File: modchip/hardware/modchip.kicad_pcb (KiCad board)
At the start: 2 copper layers, 106.2 x 37.2 mm, 4 parts, among them J1 To switch T3 (I2C slave), J2 To switch T8 (GPIO46-49), J3 To switch T5 (UART0)

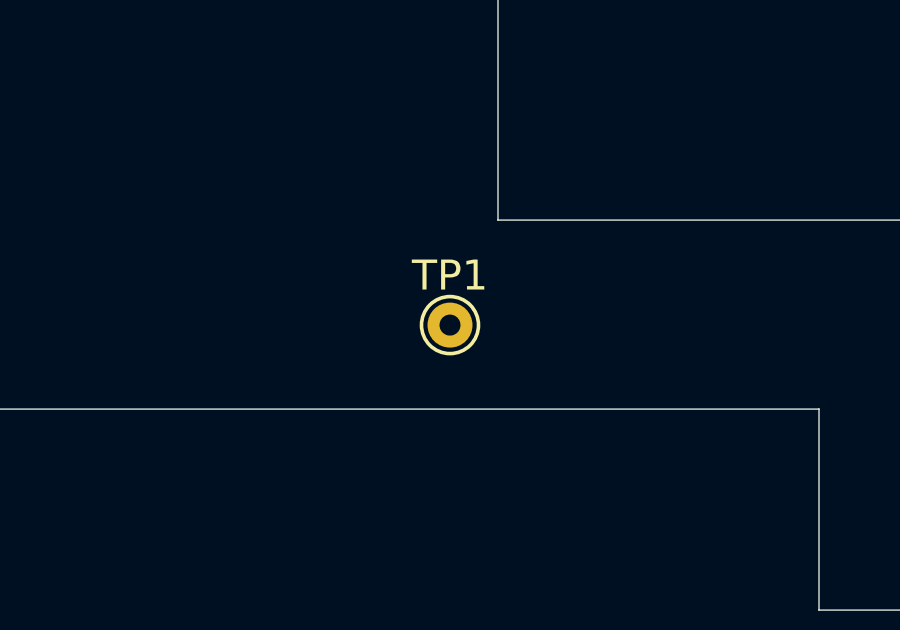
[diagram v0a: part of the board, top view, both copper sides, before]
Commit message: modchip: switch to the RP2350; wire the reset to D3's anode
The design moves from the RP2040 to the RP2350 (RP2354A, with 2 MiB of flash
in the package, or RP2350A with a W25Q16JV): a hardware RNG, SHA-256
acceleration, OTP for keys and 520 KB of SRAM make HTTPS practical. The
architecture doc covers the on-chip switching regulator's inductor, the
four-layer stack, erratum E9 and the UART divisors from a 150 MHz clk_peri.
Pin assignments are unchanged; the Pico scripts run on a Pico 2 as well.

The doc placed the reset line at D3's cathode. In this RC reset the
cathode (the banded rear end) sits on the 3.3 V rail, and pulling it low
would short the supply. The reset node is the anode, the front pad beside
the "+". The doc now says so, describes the meter check (0 ohm vs 33 kOhm
to 3.3 V), and adds 1 kOhm in series with the driver so a misplaced wire
can't short the rail. TP1 moves to 1 mm closer to the anode pad.

Co-Authored-By: Claude Opus 5.5 <noreply@anthropic.com>
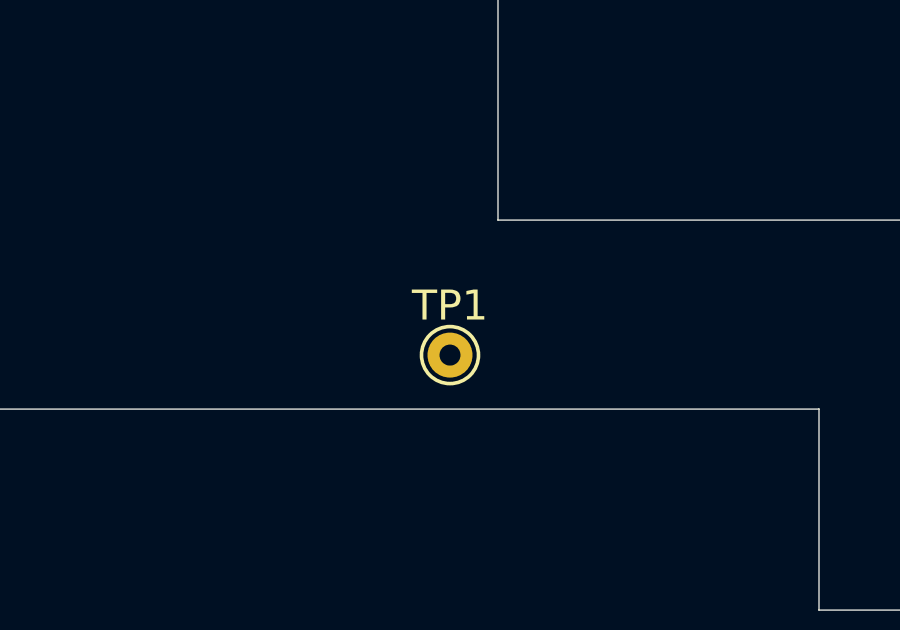
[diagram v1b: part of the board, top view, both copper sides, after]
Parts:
- TP1: value Reset wire to D3 -> Reset: wire to D3 anode (front pad, + end)
- moved TP1 1.00 mm to (120.2, 56.0)
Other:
- board text added: "TP1: wire to D3's ANODE (front pad, by the +), never the banded end (3.3 V rail). 1 k in series in the driver."

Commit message: modchip: KiCad 10 schematic of the RP2350 mod chip
make_sch.py generates modchip.kicad_sch from tables that give the net of
every pin of every part, with symbols from KiCad 10's standard library
(flattened as KiCad embeds them) and global labels named as on the board.
check_sch.py runs ERC and compares KiCad's netlist pin by pin with
expected-nets.json: all 240 pins match, and the only ERC error is the
intended one, the two LM66100 ideal diodes both driving +3V3.

The circuit: RP2354A with the core regulator from the datasheet's figure
22, a 12 MHz crystal, BOOTSEL/RUN, SWD and a status LED; USB-C with ESD
protection and an AP2112K-3.3, ORed with the switch's 3.3 V by two
LM66100; a sense divider on GP26; 100 R on every switch line, I2C
pull-ups to the switch's rail; the reset driver with 1 k to TP1.

U5 (W25Q16JVUXIQ) and C19 sit on the QSPI bus as DNP: fit them only with an
RP2350A. The RP2354A's internal flash is wired to the same QSPI pads
(RP2350 datasheet 14.3), so fitting both would put two chips on one chip
select.

make_pcb.py now links J1-J3 and TP1 to their symbols and copies their
fields, makes the board four layers and leaves J3 pin 4 open, so Update
PCB from Schematic adds the remaining parts without touching those four.

Co-Authored-By: Claude Opus 5.5 <noreply@anthropic.com>
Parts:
- J1, J2: footprint PinHeader_1x06_P2.00mm_Vertical -> Connector_PinHeader_2.00mm:PinHeader_1x06_P2.00mm_Vertical
- J3: footprint PinHeader_1x04_P2.54mm_Vertical -> Connector_PinHeader_2.54mm:PinHeader_1x04_P2.54mm_Vertical
- TP1: value Reset: wire to D3 anode (front pad, + end) -> Reset wire to D3 anode; footprint TestPoint_THTPad_D1.5mm_Drill0.7mm -> TestPoint:TestPoint_THTPad_D1.5mm_Drill0.7mm
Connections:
- J3 pad 4: +3V3_SW -> (no net)
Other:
- copper layers 2 -> 4

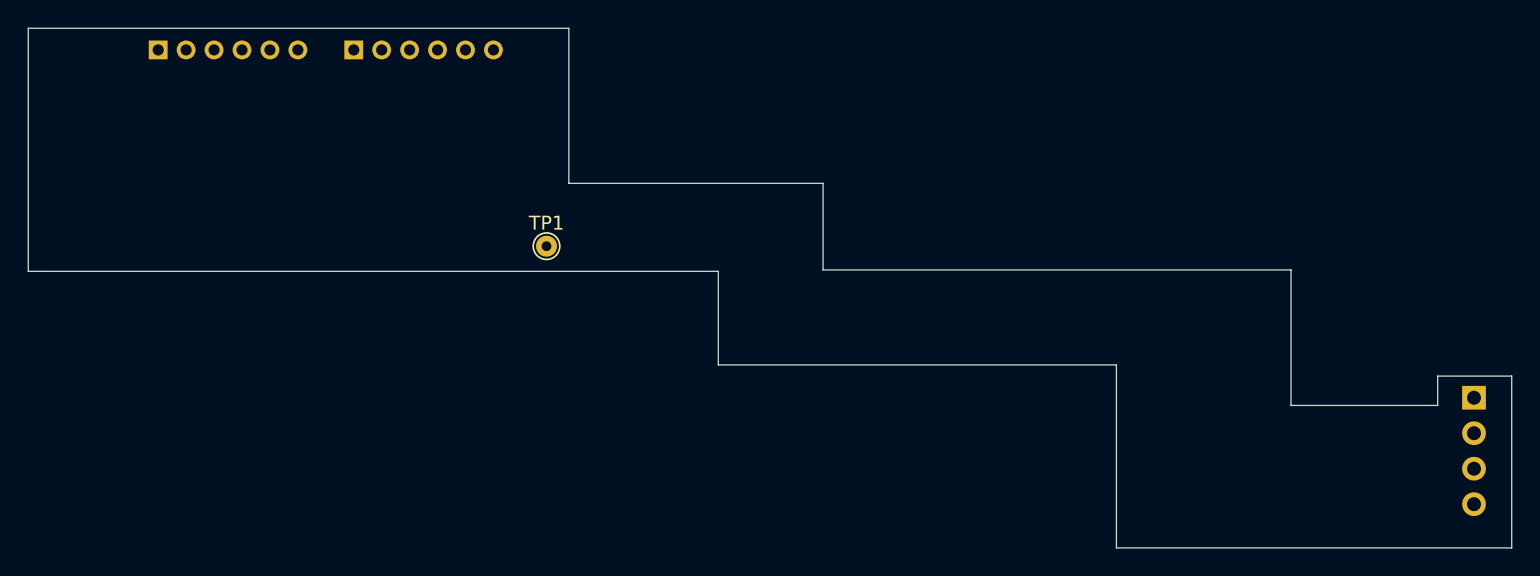
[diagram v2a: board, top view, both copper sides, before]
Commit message: modchip: route the RP2350 board and generate JLCPCB production files
Layout and routing, built by modchip/hardware/build.sh with kicad-agent-kit
(board from netlist, placement, plane fanout, Freerouting, A* finisher):

- 4 layers: F.Cu parts and signals, In1 GND, In2 +3V3, B.Cu signals; only
  the hand-soldered headers on the bottom.
- GPIOs follow the board: U1 rotated 270 puts GP11..GP0 under T3/T8 in
  header order (I2C on I2C1, GP11/GP10; T8 on GP7..GP4; UART GP0/GP1;
  reset GP27; LED GP22), so the fan-out doesn't cross.
- Hand routes laid before the router: VREG_LX and VREG_AVDD, the +3V3 trunk
  to CIN, the +1V1 DVDD pins on vias and B.Cu tracks round the exposed pad,
  the T8 fan and UART lanes, and a few boxed-in plane vias. Escape corridors
  round U1 stay clear of auto-placed parts.
- KiCad DRC: no errors, no warnings, schematic parity included.

Circuit changes on the way: no USB (SWD on J5 programs, debugs and can
power the board, the LM66100 keeping that supply out of the switch); the
RP2350A with a W25Q128JVSIQ is the default build, an RP2354A without U5/C19
the alternative; every part has an LCSC number, Basic wherever one exists,
with four in-stock Extended parts (RP2350A, LM66100, the datasheet's AOTA
inductor, the ABM8 crystal the RP2350 is tuned for); headers are not
assembled. Fixed on the way: L1's fields were passed as its DNP flag.

production/ holds the Gerber/drill zip, BOM (19 lines) and placement file
(48 parts, top side only) from the Fabrication Toolkit.

Co-Authored-By: Claude Opus 5.5 <noreply@anthropic.com>
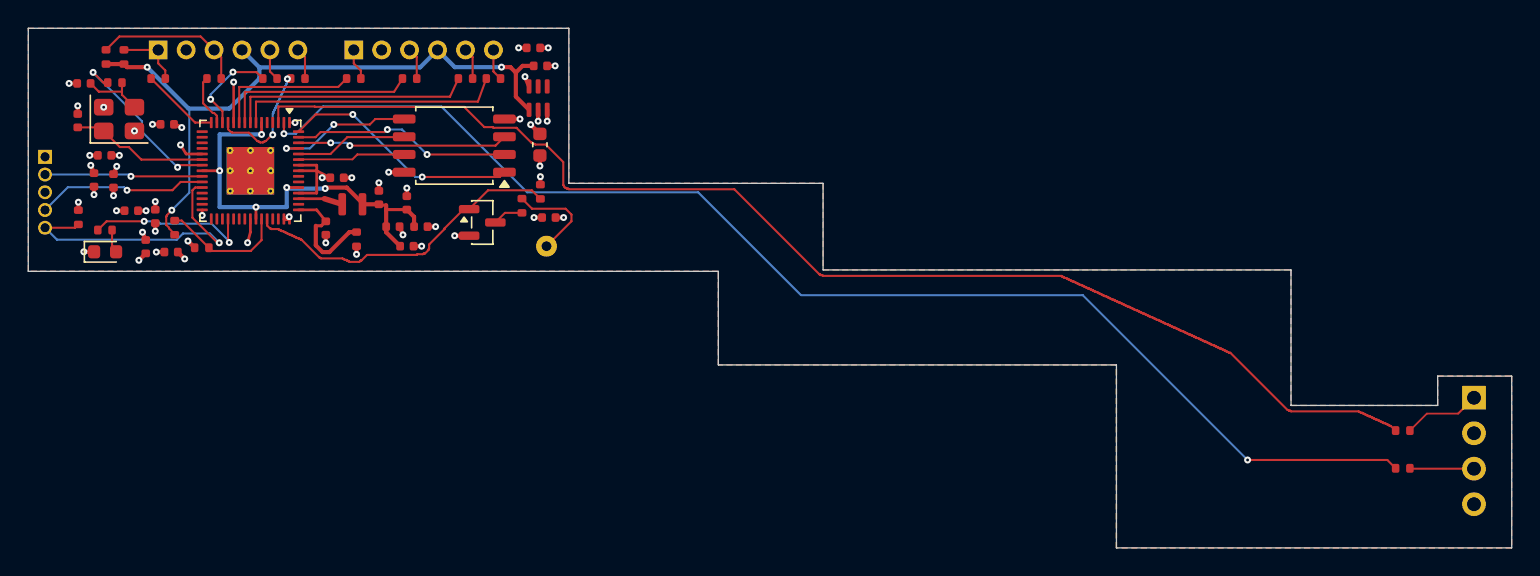
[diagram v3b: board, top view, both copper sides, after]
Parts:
- added C1: 100n, Capacitor_SMD:C_0402_1005Metric, F.Cu at (120.4, 53.9)
- added C10: 100n, Capacitor_SMD:C_0402_1005Metric, F.Cu at (109.2, 54.6)
- added C11: 100n, Capacitor_SMD:C_0402_1005Metric, F.Cu at (111.2, 54.6)
- added C12: 100n, Capacitor_SMD:C_0402_1005Metric, F.Cu at (110.2, 56.0)
- added C13: 4.7u, Capacitor_SMD:C_0402_1005Metric, F.Cu at (105.2, 51.1)
- added C14: 4.7u, Capacitor_SMD:C_0402_1005Metric, F.Cu at (108.2, 52.5)
- added C15: 4.7u, Capacitor_SMD:C_0402_1005Metric, F.Cu at (110.2, 52.9)
- added C16: 4.7u, Capacitor_SMD:C_0402_1005Metric, F.Cu at (104.4, 54.7)
- added C17: 15p, Capacitor_SMD:C_0402_1005Metric, F.Cu at (86.6, 47.0)
- added C18: 15p, Capacitor_SMD:C_0402_1005Metric, F.Cu at (87.1, 44.3)
- added C19: 100n, Capacitor_SMD:C_0402_1005Metric, F.Cu at (119.3, 41.8)
- added C2: 100n, Capacitor_SMD:C_0402_1005Metric, F.Cu at (87.8, 51.3)
- added C22: 10u, Capacitor_SMD:C_0603_1608Metric, F.Cu at (119.7, 48.7)
- added C24: 1u, Capacitor_SMD:C_0402_1005Metric, F.Cu at (119.8, 43.1)
- added C3: 100n, Capacitor_SMD:C_0402_1005Metric, F.Cu at (88.6, 49.5)
- added C4: 100n, Capacitor_SMD:C_0402_1005Metric, F.Cu at (89.2, 51.3)
- added C5: 100n, Capacitor_SMD:C_0402_1005Metric, F.Cu at (91.5, 56.0)
- added C6: 100n, Capacitor_SMD:C_0402_1005Metric, F.Cu at (93.3, 56.4)
- added C7: 100n, Capacitor_SMD:C_0402_1005Metric, F.Cu at (90.5, 53.5)
- added C8: 100n, Capacitor_SMD:C_0402_1005Metric, F.Cu at (92.2, 53.9)
- added C9: 100n, Capacitor_SMD:C_0402_1005Metric, F.Cu at (93.1, 47.3)
- added D1: red, LED_SMD:LED_0603_1608Metric, F.Cu at (88.6, 56.4)
- added J5: SWD, Connector_PinHeader_1.27mm:PinHeader_1x05_P1.27mm_Vertical, F.Cu at (84.3, 49.6)
- added L1: 3.3uH, Inductor_SMD:L_Murata_DFE201610P, F.Cu at (106.3, 53.0)
- added Q1: 2N7002, Package_TO_SOT_SMD:SOT-23, F.Cu at (115.6, 54.3)
- added R10: 100, Resistor_SMD:R_0402_1005Metric, F.Cu at (181.5, 71.9)
- added R11: 100, Resistor_SMD:R_0402_1005Metric, F.Cu at (181.5, 69.2)
- added R12: 100, Resistor_SMD:R_0402_1005Metric, F.Cu at (96.4, 44.0)
- added R13: 100, Resistor_SMD:R_0402_1005Metric, F.Cu at (92.4, 44.0)
- added R14: 100, Resistor_SMD:R_0402_1005Metric, F.Cu at (100.4, 44.0)
- added R15: 100, Resistor_SMD:R_0402_1005Metric, F.Cu at (102.4, 44.0)
- added R16: 100, Resistor_SMD:R_0402_1005Metric, F.Cu at (106.4, 44.0)
- added R17: 100, Resistor_SMD:R_0402_1005Metric, F.Cu at (114.4, 44.0)
- added R18: 100, Resistor_SMD:R_0402_1005Metric, F.Cu at (110.4, 44.0)
- added R19: 100, Resistor_SMD:R_0402_1005Metric, F.Cu at (116.4, 44.0)
- added R20: 4.7k, Resistor_SMD:R_0402_1005Metric, F.Cu at (88.7, 42.5)
- added R21: 4.7k, Resistor_SMD:R_0402_1005Metric, F.Cu at (90.0, 42.5)
- added R22: 100k, Resistor_SMD:R_0402_1005Metric, F.Cu at (93.6, 54.7)
- added R23: 100k, Resistor_SMD:R_0402_1005Metric, F.Cu at (95.5, 56.1)
- added R24: 100k, Resistor_SMD:R_0402_1005Metric, F.Cu at (119.8, 52.1)
- added R25: 1k, Resistor_SMD:R_0402_1005Metric, F.Cu at (118.4, 53.1)
- added R5: 33, Resistor_SMD:R_0402_1005Metric, F.Cu at (106.6, 55.5)
- added R6: 1k, Resistor_SMD:R_0402_1005Metric, F.Cu at (89.3, 44.3)
- added R8: 10k, Resistor_SMD:R_0402_1005Metric, F.Cu at (86.7, 53.9)
- added R9: 330, Resistor_SMD:R_0402_1005Metric, F.Cu at (88.6, 54.8)
- added U1: RP2350A, Package_DFN_QFN:QFN-60-1EP_7x7mm_P0.4mm_EP3.4x3.4mm_ThermalVias, F.Cu at (99.0, 50.6)
- added U2: LM66100, Package_TO_SOT_SMD:SOT-363_SC-70-6, F.Cu at (119.6, 45.4)
- added U5: W25Q128JVSIQ, Package_SO:SOIC-8_5.3x5.3mm_P1.27mm, F.Cu at (113.6, 48.8)
- added Y1: 12MHz, Crystal:Crystal_SMD_3225-4Pin_3.2x2.5mm, F.Cu at (89.6, 46.9)
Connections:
- J3 pad 4: (no net) -> unconnected-(J3-Pin_4-Pad4)
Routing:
- net UART_TX: track 0.00 -> 91.9 mm, vias 0 -> 2
- net UART_RX: track 0.00 -> 91.4 mm
- net +3V3_SW: track 0.00 -> 49.5 mm, vias 0 -> 3
- net +1V1: track 0.00 -> 32.2 mm, vias 0 -> 5
- net +3V3: track 0.00 -> 25.5 mm, vias 0 -> 22
- net RESET_DRV: track 0.00 -> 22.6 mm
- net RUN: track 0.00 -> 21.2 mm, vias 0 -> 1
- net T8_GPIO49: track 0.00 -> 19.1 mm
- net GND: track 0.00 -> 18.5 mm, vias 0 -> 30
- net T8_GPIO47: track 0.00 -> 17.6 mm
- net QSPI_SS: track 0.00 -> 17.2 mm, vias 0 -> 2
- net QSPI_SD1: track 0.00 -> 15.7 mm, vias 0 -> 2
- net QSPI_SD2: track 0.00 -> 15.1 mm, vias 0 -> 2
- net T8_GPIO48: track 0.00 -> 14.0 mm
- net XOUT: track 0.00 -> 12.5 mm, vias 0 -> 2
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- added copper zone on In2.Cu, net +3V3
- added copper zone on B.Cu, net GND
- added copper zone on F.Cu, net GND
- added copper zone on In1.Cu, net GND
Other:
- board text added: "Header holes measured on a photo (+/-0.3 mm): check them with calipers before ordering."
- board text added: "TP1: wire to D3's ANODE (front pad, by the +), never the banded end (3.3 V rail)."
- board text added: "U1 RP2350A + U5 W25Q128JVSIQ (default); for an RP2354A build leave U5 and C19 off."
- board text removed: "Keep the bottom side free of other parts: SMD parts on the switch sit up to 3 mm below it."
- board text removed: "Origin (aux, grid) at T3 pin 1. Positions +/-0.3 mm from a photo: verify before ordering."
- board text removed: "TP1: wire to D3's ANODE (front pad, by the +), never the banded end (3.3 V rail). 1 k in series in the driver."
